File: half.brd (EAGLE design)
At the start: 110 x 91 mm, 112 parts, among them IC1 TLC59711, IC2 TLC59711, IC3 TLC59711, IC4 74HC08D, J2 AUDIO_JACK_TRRSCUI, J3 AUDIO_JACK_TRRSCUI, J4 FEMALE 2x3, J5 FEMALE 2x3, SW11 CHERRY-MX-LEDSMD, SW12 CHERRY-MX-LEDSMD, SW13 CHERRY-MX-LEDSMD, SW14 CHERRY-MX-LEDSMD, SW15 CHERRY-MX-LEDSMD, SW16 CHERRY-MX-LEDSMD, SW21 CHERRY-MX-LEDSMD, SW22 CHERRY-MX-LEDSMD, SW23 CHERRY-MX-LEDSMD, SW24 CHERRY-MX-LEDSMD, SW25 CHERRY-MX-LEDSMD, SW26 CHERRY-MX-LEDSMD, SW31 CHERRY-MX-LEDSMD, SW32 CHERRY-MX-LEDSMD, SW33 CHERRY-MX-LEDSMD, SW34 CHERRY-MX-LEDSMD, SW35 CHERRY-MX-LEDSMD, SW36 CHERRY-MX-LEDSMD, SW41 CHERRY-MX-LEDSMD, SW42 CHERRY-MX-LEDSMD, SW43 CHERRY-MX-LEDSMD, SW44 CHERRY-MX-LEDSMD, SW45 CHERRY-MX-LEDSMD, SW46 CHERRY-MX-LEDSMD, SW51 CHERRY-MX-LEDSMD, SW52 CHERRY-MX-LEDSMD, SW53 CHERRY-MX-LEDSMD, SW54 CHERRY-MX-LEDSMD, SW55 CHERRY-MX-LEDSMD, SW56 CHERRY-MX-LEDSMD, U1 MBT40, U2 SPX3819-3.3, U3 MCP73831T-2ACI/OT, U4 32U4, Y1 8MHz

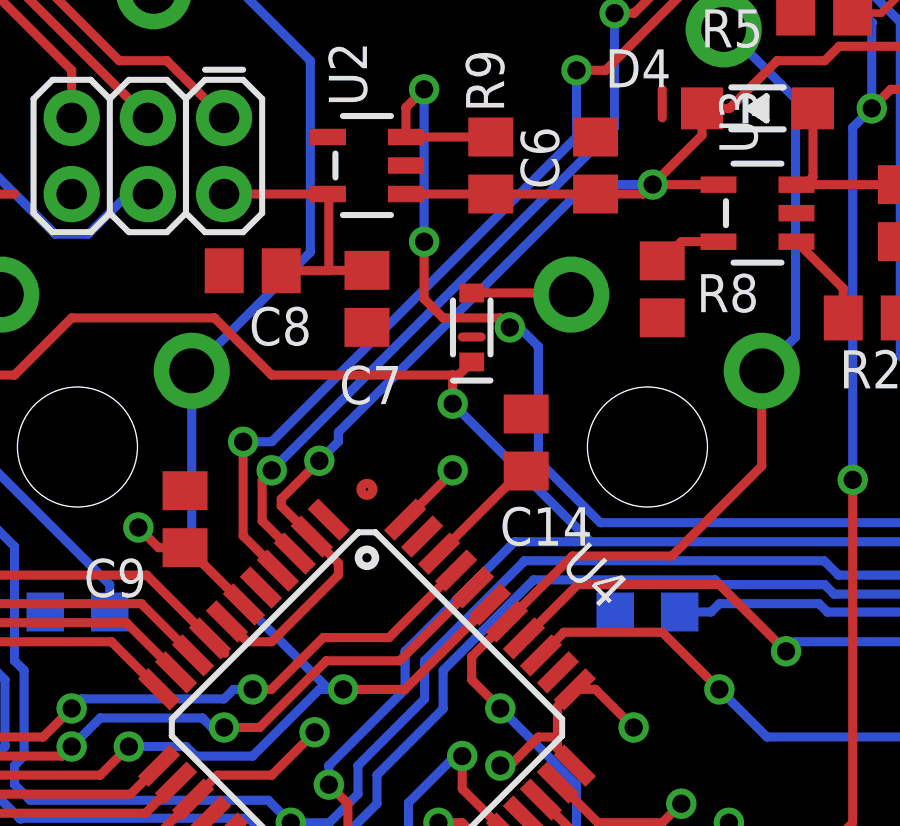
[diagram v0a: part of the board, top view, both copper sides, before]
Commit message: Disconnect UVCC on 32u4 to reflect a greenwire fix on PCB
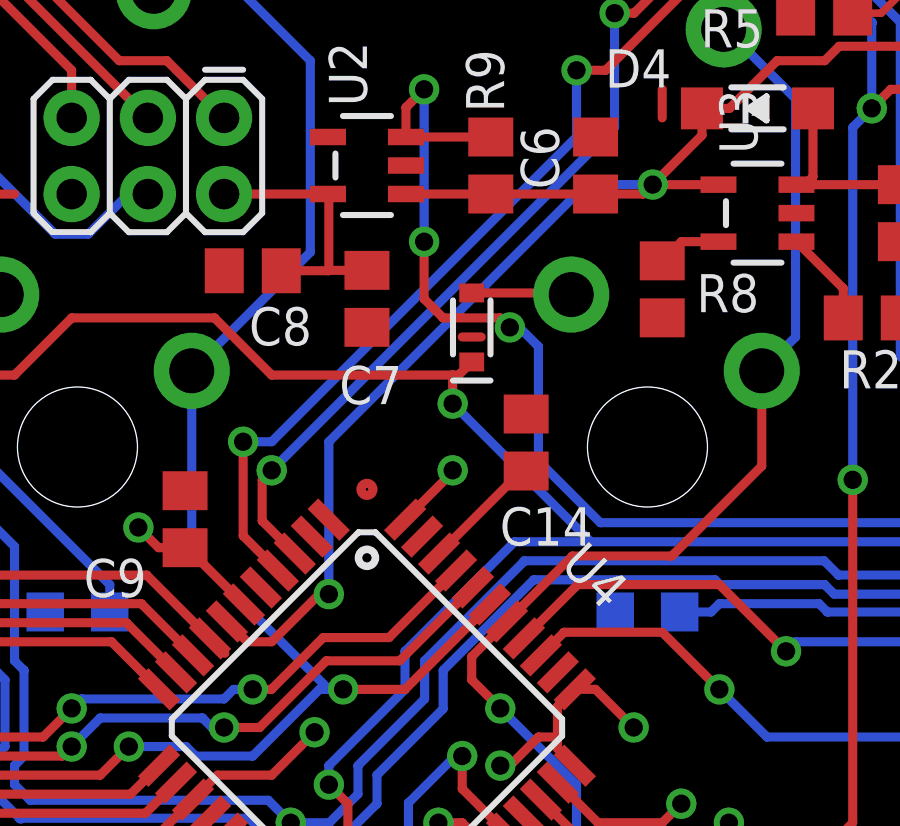
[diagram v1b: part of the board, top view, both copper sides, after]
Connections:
- net VBUS: no longer U4.2
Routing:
- net VBUS: track 70.7 -> 69.0 mm
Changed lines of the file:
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@@
 <layer number="20" name="Dimension" color="15" fill="1" visible="yes" active="yes"/>
 <layer number="21" name="tPlace" color="14" fill="1" visible="yes" active="yes"/>
-<layer number="22" name="bPlace" color="14" fill="1" visible="yes" active="yes"/>
+<layer number="22" name="bPlace" color="14" fill="1" visible="no" active="yes"/>
 <layer number="23" name="tOrigins" color="14" fill="1" visible="yes" active="yes"/>
-<layer number="24" name="bOrigins" color="13" fill="1" visible="yes" active="yes"/>
+<layer number="24" name="bOrigins" color="13" fill="1" visible="no" active="yes"/>
 <layer number="25" name="tNames" color="7" fill="1" visible="no" active="yes"/>
 <layer number="26" name="bNames" color="7" fill="1" visible="no" active="yes"/>
@@
 <wire x1="77.452675" y1="87.10268125" x2="77.452675" y2="86.501425" width="0.3048" layer="1"/>
 <wire x1="77.452675" y1="86.501425" x2="77.202675" y2="86.251425" width="0.3048" layer="1"/>
-<contactref element="U4" pad="2"/>
 <wire x1="77.452675" y1="87.10268125" x2="77.452675" y2="89.869825" width="0.3048" layer="1"/>
 <wire x1="75.2475" y1="91.1225" x2="74.295" y2="90.17" width="0.3048" layer="1"/>
@@
 <wire x1="64.77" y1="74.9325" x2="61.2775" y2="74.9325" width="0.3048" layer="1"/>
 <wire x1="58.4501" y1="74.9325" x2="61.2775" y2="74.9325" width="0.3048" layer="1"/>
-<wire x1="55.311521875" y1="63.513959375" x2="54.2925" y2="64.53298125" width="0.3048" layer="1"/>
-<wire x1="54.2925" y1="64.53298125" x2="54.2925" y2="64.77" width="0.3048" layer="1"/>
-<wire x1="54.2925" y1="64.77" x2="55.5625" y2="66.04" width="0.3048" layer="1"/>
-<via x="55.5625" y="66.04" extent="1-16" drill="0.6096"/>
+<via x="55.88" y="61.595" extent="1-16" drill="0.6096"/>
 <wire x1="53.161125" y1="60.0075" x2="52.48309375" y2="60.68553125" width="0.3048" layer="1"/>
-<wire x1="53.975" y1="60.0075" x2="53.161125" y2="60.0075" width="0.3048" layer="1"/>
-<wire x1="56.1975" y1="62.23" x2="53.975" y2="60.0075" width="0.3048" layer="1"/>
-<wire x1="55.311521875" y1="63.513959375" x2="56.1975" y2="62.62798125" width="0.3048" layer="1"/>
-<wire x1="56.1975" y1="62.62798125" x2="56.1975" y2="62.23" width="0.3048" layer="1"/>
-<wire x1="55.5625" y1="66.3575" x2="55.5625" y2="66.04" width="0.3048" layer="16"/>
+<wire x1="53.161125" y1="60.0075" x2="53.975" y2="60.0075" width="0.3048" layer="1"/>
 <wire x1="77.3811" y1="81.95521875" x2="77.3811" y2="81.23978125" width="0.3048" layer="1"/>
 <wire x1="77.3811" y1="81.23978125" x2="75.99821875" y2="79.8569" width="0.3048" layer="1"/>
@@
 <wire x1="66.6775" y1="75.245" x2="68.8674" y2="75.245" width="0.3048" layer="1"/>
 <wire x1="66.675" y1="75.2475" x2="68.3175" y2="76.89" width="0.3048" layer="1"/>
-<wire x1="55.5625" y1="66.04" x2="56.1975" y2="66.675" width="0.3048" layer="16"/>
-<wire x1="56.1975" y1="66.675" x2="56.1975" y2="66.9925" width="0.3048" layer="16"/>
-<wire x1="56.1975" y1="66.9925" x2="64.4525" y2="75.2475" width="0.3048" layer="16"/>
-<wire x1="64.4525" y1="75.2475" x2="66.675" y2="75.2475" width="0.3048" layer="16"/>
+<wire x1="66.675" y1="75.2475" x2="64.4525" y2="75.2475" width="0.3048" layer="16"/>
 <wire x1="75.99821875" y1="79.8569" x2="72.8894" y2="79.8569" width="0.3048" layer="1"/>
 <wire x1="72.8894" y1="79.8569" x2="72.4075" y2="79.375" width="0.3048" layer="1"/>
@@
 <wire x1="69.2325" y1="77.7875" x2="68.3175" y2="77.7875" width="0.3048" layer="1"/>
 <wire x1="68.3175" y1="76.89" x2="68.3175" y2="77.7875" width="0.3048" layer="1"/>
+<wire x1="55.5625" y1="61.595" x2="55.88" y2="61.595" width="0.3048" layer="1"/>
+<wire x1="53.975" y1="60.0075" x2="55.5625" y2="61.595" width="0.3048" layer="1"/>
+<wire x1="55.88" y1="66.675" x2="55.88" y2="61.595" width="0.3048" layer="16"/>
+<wire x1="64.4525" y1="75.2475" x2="55.88" y2="66.675" width="0.3048" layer="16"/>
 </signal>
 <signal name="VBAT">
